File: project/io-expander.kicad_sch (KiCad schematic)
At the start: 0 parts

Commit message: Added CubeMX project and some schematic components are added
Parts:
- added IC5: MCP23017-E_ML, QFN65P600X600X100-29N-D, symbol bozi:MCP23017-E_ML
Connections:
- new net 3V3_AO: IC5.5 (VDD)
- new net GNDREF: IC5.29 (EP), IC5.6 (VSS)
- new net GPA0: IC5.17 (GPA0)
- new net GPA1: IC5.18 (GPA1)
- new net GPA2: IC5.19 (GPA2)
- new net GPA3: IC5.20 (GPA3)
- new net GPA4: IC5.21 (GPA4)
- new net GPA5: IC5.22 (GPA5)
- new net GPA6: IC5.23 (GPA6)
- new net GPA7: IC5.24 (GPA7)
- new net GPB0: IC5.25 (GPB0)
- new net GPB1: IC5.26 (GPB1)
- new net GPB2: IC5.27 (GPB2)
- new net GPB3: IC5.28 (GPB3)
- new net GPB4: IC5.1 (GPB4)
- new net GPB5: IC5.2 (GPB5)
- new net GPB6: IC5.3 (GPB6)
- new net GPB7: IC5.4 (GPB7)
- new net I2C_SCL: IC5.8 (SCL)
- new net I2C_SDA: IC5.9 (SDA)
- new net INTA: IC5.16 (INTA)
- new net INTB: IC5.15 (INTB)
- new net ~{RESET}: IC5.14 (~{RESET})
- no-connect marks 0 -> 2

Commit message: schemtic is done, need to go through BOM
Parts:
- added C122, C125: 100nF, bozi:GRM18_T10, symbol Device:C
- added C123: 1uF, bozi:GRM15_T05, symbol Device:C
- added D10: TBD, symbol Device:D
- added D7, D8, D9: LED, bozi:LEDC1608X70N_edit, symbol Device:LED
- added J3: POGO header 20 pin, symbol bozi:POGO_20P
- added R35, R36, R37, R43: 100R, bozi:RESC1005X37N_edit, symbol Device:R
- added R38, R39, R40, R41: 1K, bozi:RESC1005X37N_edit, symbol Device:R
- added R42, R44, R45, R46: 10K, bozi:RESC1005X37N_edit, symbol Device:R
- added SW2: SW_DIP_x04, bozi:2194MST_edit, symbol Switch:SW_DIP_x04
- added SW3: PTS636SM43SMTR LFS, bozi:PTS636SM43SMTRLFS_edit, symbol Switch:SW_Push
- IC5: footprint QFN65P600X600X100-29N-D -> bozi:QFN65P600X600X100-29N-D_edit; Manufacturer_Name Microchip -> Microchip Technology
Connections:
- net INTB is gone; now on net IO_EX_INT: IC5.15 (INTB)
- net 3V3_AO: now also C123.1, C125.1, R44.2
- net GNDREF: now also C122.2, C123.2, C125.2, D10.2 (A), D7.1 (K), D8.1 (K), D9.1 (K), J3.15, J3.16, J3.5, J3.7, R43.2, R45.2, R46.2, SW3.2
- net at IC5.11 (A0): now also R44.1
- net at IC5.12 (A1): now also R45.1
- net at IC5.13 (A2): now also R46.1
- net GPA6 renamed LD1
- net LD1: now also R35.1
- net GPA7 renamed LD2
- net LD2: now also R36.1
- net GPB6 renamed DIP1
- net DIP1: now also SW2.5
- net GPB7 renamed LD3
- net LD3: now also R37.1
- net I2C_SCL renamed IO_EX_I2C_SCL
- net I2C_SDA renamed IO_EX_I2C_SDA
- net INTA renamed IO_EX_INT
- net ~{RESET} renamed NRST
- net NRST: now also C122.1, D10.1 (K), J3.12, R42.2, SW3.1
- new net: R41.2, SW2.4
- new net: D9.2 (A), R37.2
- new net: D7.2 (A), R35.2
- new net: J3.11, R43.1
- new net: R40.2, SW2.3
- new net: D8.2 (A), R36.2
- new net: R38.2, SW2.1
- new net: R39.2, SW2.2
- new net BOOT0: SW2.8
- new net BOOT1: SW2.7
- new net BOOT2: SW2.6
- new net T_JCLK/T_SWCLK: J3.6
- new net T_JTDI: J3.10
- new net T_JTDO/T_SWO: J3.8
- new net T_JTMS/T_SWDIO: J3.4
- new net T_VCP_RX: J3.13
- new net T_VCP_TX: J3.14
- new net UART_CTS: J3.17
- new net UART_RTS: J3.19
- new net UART_RX: J3.20
- new net UART_TX: J3.18
- new net VDD: J3.3, R38.1, R39.1, R40.1, R41.1, R42.1
- no-connect marks 2 -> 5
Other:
- note added: "BOOT options"
- note added: "GPA7 and GPB7 are output only"
- note added: "POGO header"
- note added: "Reset button"
- note added: "User LEDs"
- moved on the sheet: IC5

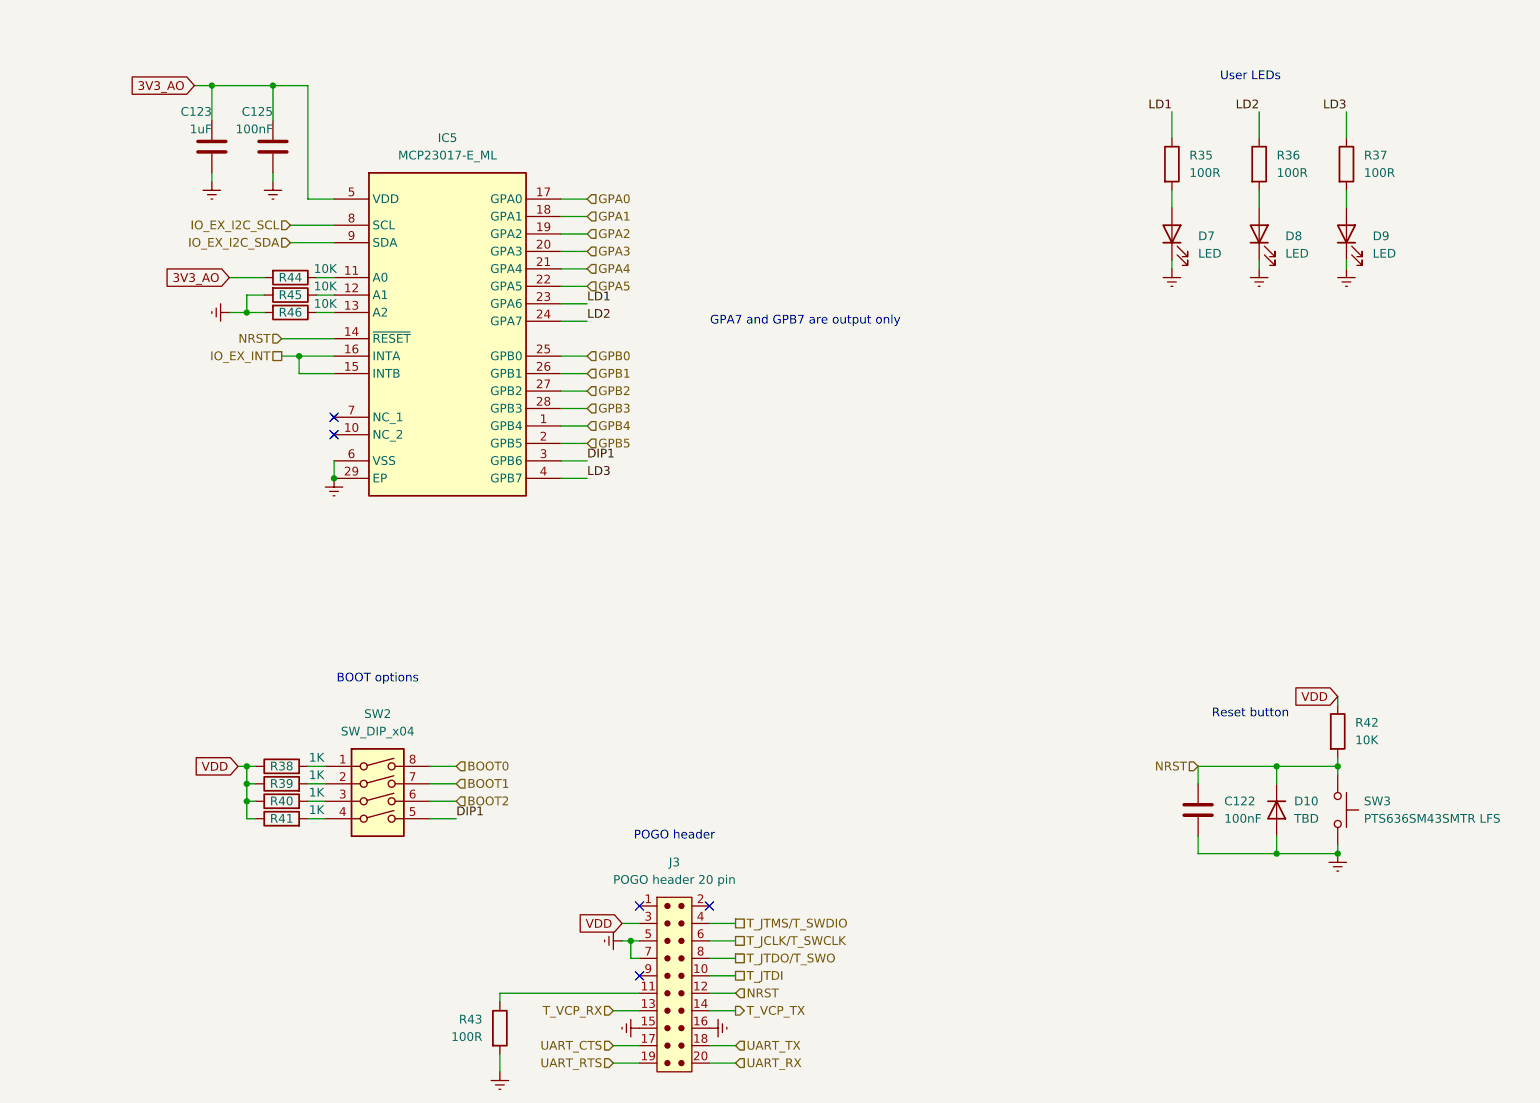
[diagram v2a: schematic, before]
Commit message: schemtic is done, annotation set
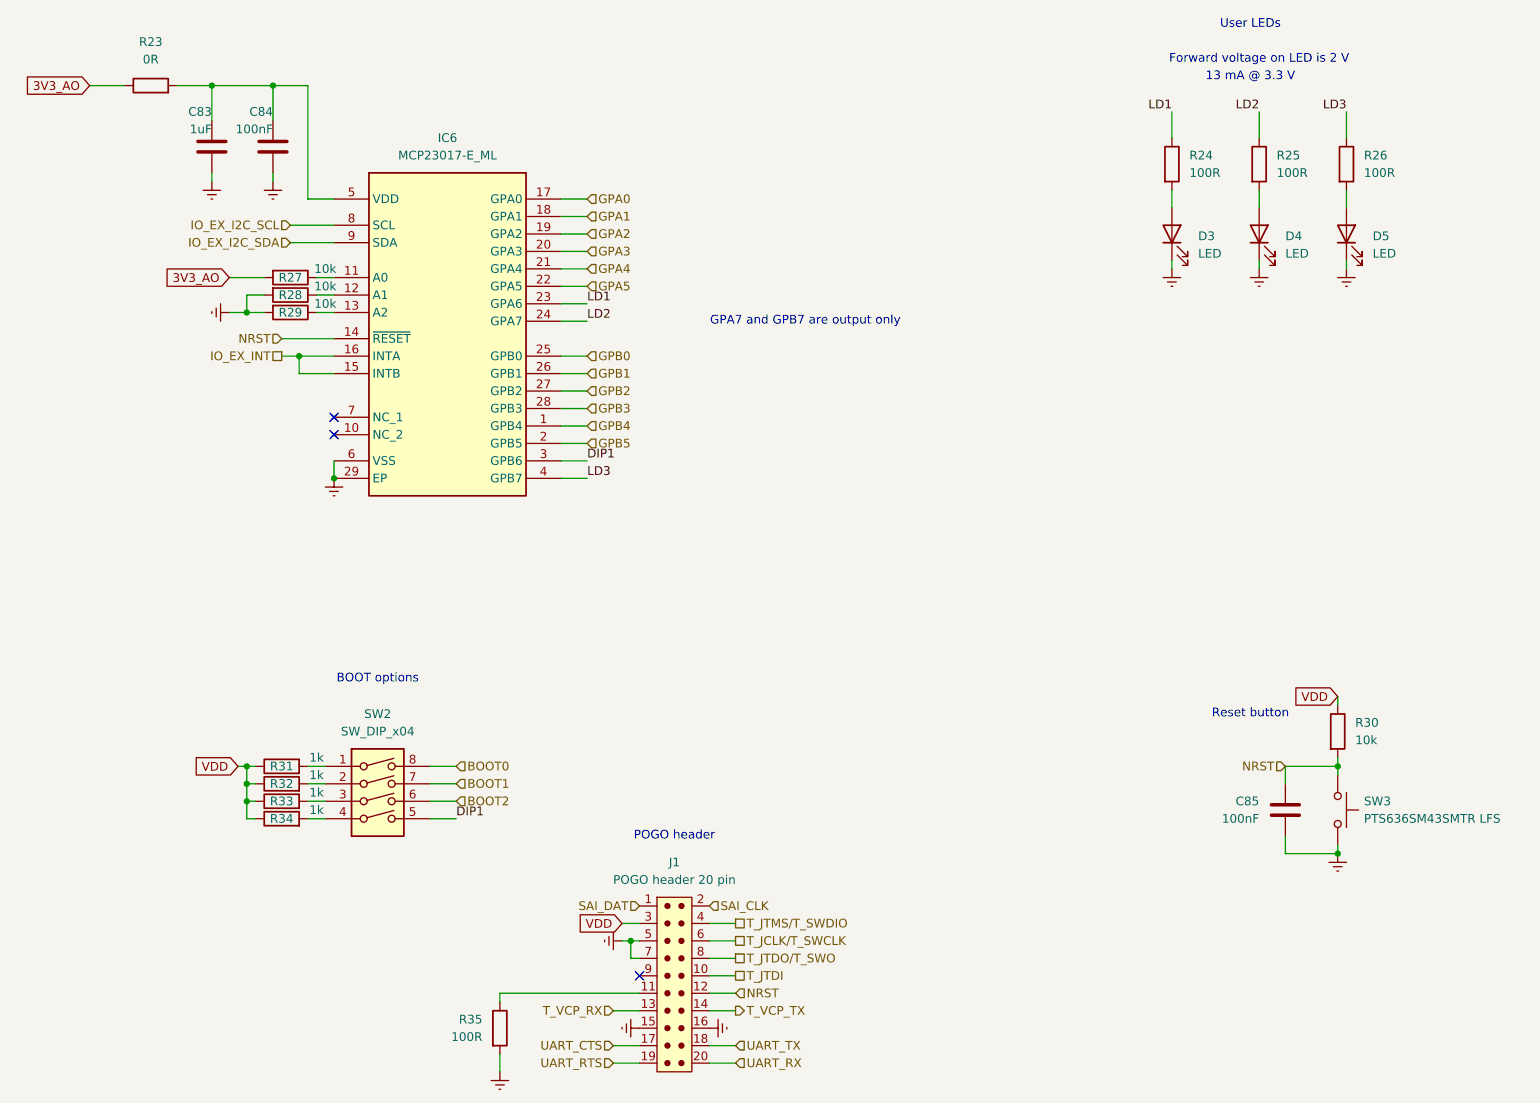
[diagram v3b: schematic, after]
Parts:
- removed D10: TBD, symbol Device:D
- added R23: 0R, bozi:RESC1005X37N_edit, symbol Device:R
- J1: renamed from J3; footprint (none) -> bozi:8552202030001101_edit; Manufacturer_Name (none) -> Mill-Max Manufacturing Corp.; Manufacturer_Part_Number (none) -> 855-22-020-30-001101
- R27: renamed from R44; value 10K -> 10k
- R28: renamed from R45; value 10K -> 10k
- R29: renamed from R46; value 10K -> 10k
- R30: renamed from R42; value 10K -> 10k
- R31: renamed from R38; value 1K -> 1k
- R32: renamed from R39; value 1K -> 1k
- R33: renamed from R40; value 1K -> 1k
- R34: renamed from R41; value 1K -> 1k
- renumbered C123 to C83, C125 to C84, C122 to C85, D7 to D3, D8 to D4, D9 to D5, IC5 to IC6, R35 to R24, R36 to R25, R37 to R26, R43 to R35
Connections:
- net 3V3_AO: now also R23.1; no longer C83.1, C84.1, IC6.5 (VDD)
- net SAI_DAT: now reaches J1.1
- net SAI_CLK: now reaches J1.2
- new net: C83.1, C84.1, IC6.5 (VDD), R23.2
- no-connect marks 5 -> 3
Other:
- note added: "13 mA @ 3.3 V"
- note added: "Forward voltage on LED is 2 V"
- moved on the sheet: C85

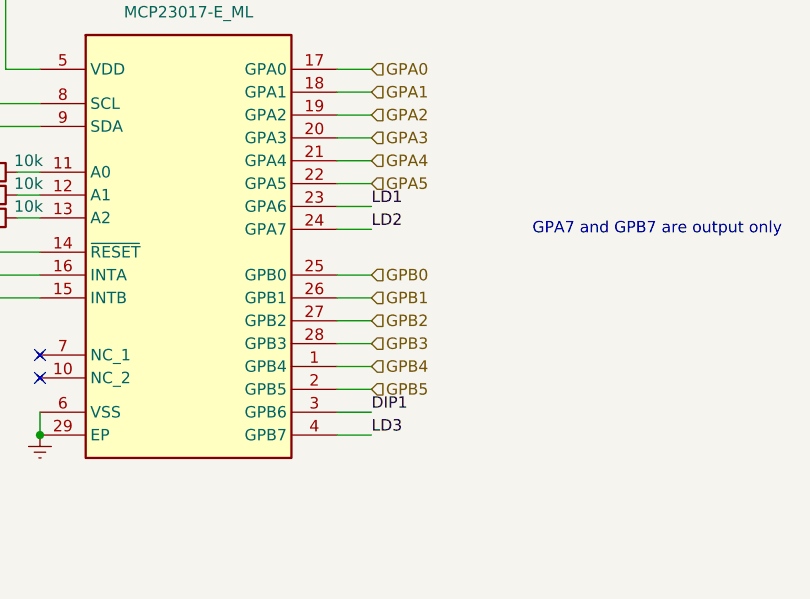
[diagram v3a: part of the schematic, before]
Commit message: PCB design, finished RAM, audio, battery fuel gauge and charger, PMIC, USB C power
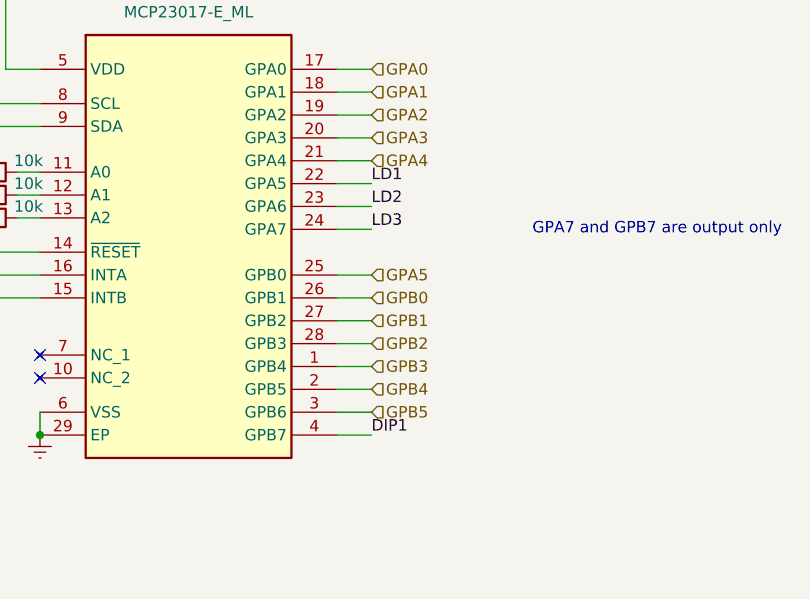
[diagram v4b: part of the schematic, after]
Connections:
- net DIP1: now also IC6.4 (GPB7); no longer IC6.3 (GPB6)
- net GPA5: now also IC6.25 (GPB0); no longer IC6.22 (GPA5)
- net GPB0: now also IC6.26 (GPB1); no longer IC6.25 (GPB0)
- net GPB1: now also IC6.27 (GPB2); no longer IC6.26 (GPB1)
- net GPB2: now also IC6.28 (GPB3); no longer IC6.27 (GPB2)
- net GPB3: now also IC6.1 (GPB4); no longer IC6.28 (GPB3)
- net GPB4: now also IC6.2 (GPB5); no longer IC6.1 (GPB4)
- net GPB5: now also IC6.3 (GPB6); no longer IC6.2 (GPB5)
- net LD1: now also IC6.22 (GPA5); no longer IC6.23 (GPA6)
- net LD2: now also IC6.23 (GPA6); no longer IC6.24 (GPA7)
- net LD3: now also IC6.24 (GPA7); no longer IC6.4 (GPB7)
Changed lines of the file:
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@@
 	)
 	(label "LD1"
+		(at 100.33 57.15 0)
+		(effects
+			(font
+				(size 1.27 1.27)
+			)
+			(justify left bottom)
+		)
+	)
+	(label "LD2"
 		(at 100.33 59.69 0)
-		(effects
-			(font
-				(size 1.27 1.27)
-			)
-			(justify left bottom)
-		)
-	)
-	(label "LD2"
-		(at 100.33 62.23 0)
 		(effects
 			(font
@@
 	)
 	(label "LD3"
+		(at 100.33 62.23 0)
+		(effects
+			(font
+				(size 1.27 1.27)
+			)
+			(justify left bottom)
+		)
+	)
+	(label "DIP1"
 		(at 100.33 85.09 0)
-		(effects
-			(font
-				(size 1.27 1.27)
-			)
-			(justify left bottom)
-		)
-	)
-	(label "DIP1"
-		(at 100.33 82.55 0)
 		(effects
 			(font
@@
 	(hierarchical_label "GPB1"
 		(shape input)
-		(at 100.33 69.85 0)
+		(at 100.33 72.39 0)
 		(effects
 			(font
@@
 	(hierarchical_label "GPB2"
 		(shape input)
-		(at 100.33 72.39 0)
+		(at 100.33 74.93 0)
 		(effects
 			(font
@@
 	(hierarchical_label "GPB5"
 		(shape input)
-		(at 100.33 80.01 0)
+		(at 100.33 82.55 0)
 		(effects
 			(font
@@
 	(hierarchical_label "GPB3"
 		(shape input)
-		(at 100.33 74.93 0)
+		(at 100.33 77.47 0)
 		(effects
 			(font
@@
 	(hierarchical_label "GPB4"
 		(shape input)
-		(at 100.33 77.47 0)
+		(at 100.33 80.01 0)
 		(effects
 			(font
@@
 	(hierarchical_label "GPB0"
 		(shape input)
+		(at 100.33 69.85 0)
+		(effects
+			(font
+				(size 1.27 1.27)
+			)
+			(justify left)
+		)
+	)
+	(hierarchical_label "GPA5"
+		(shape input)
 		(at 100.33 67.31 0)
 		(effects
 			(font
-				(size 1.27 1.27)
-			)
-			(justify left)
-		)
-	)
-	(hierarchical_label "GPA5"
-		(shape input)
-		(at 100.33 57.15 0)
-		(effects
-			(font
